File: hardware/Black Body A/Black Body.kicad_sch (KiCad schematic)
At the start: 33 parts, among them IC2 MCP96L00T-E_MX, J1 53307-2471, J2 Conn_01x02, J4 LogicAnalyzer, J5 Conn_02x04_Top_Bottom, J7 Conn_02x03_Top_Bottom

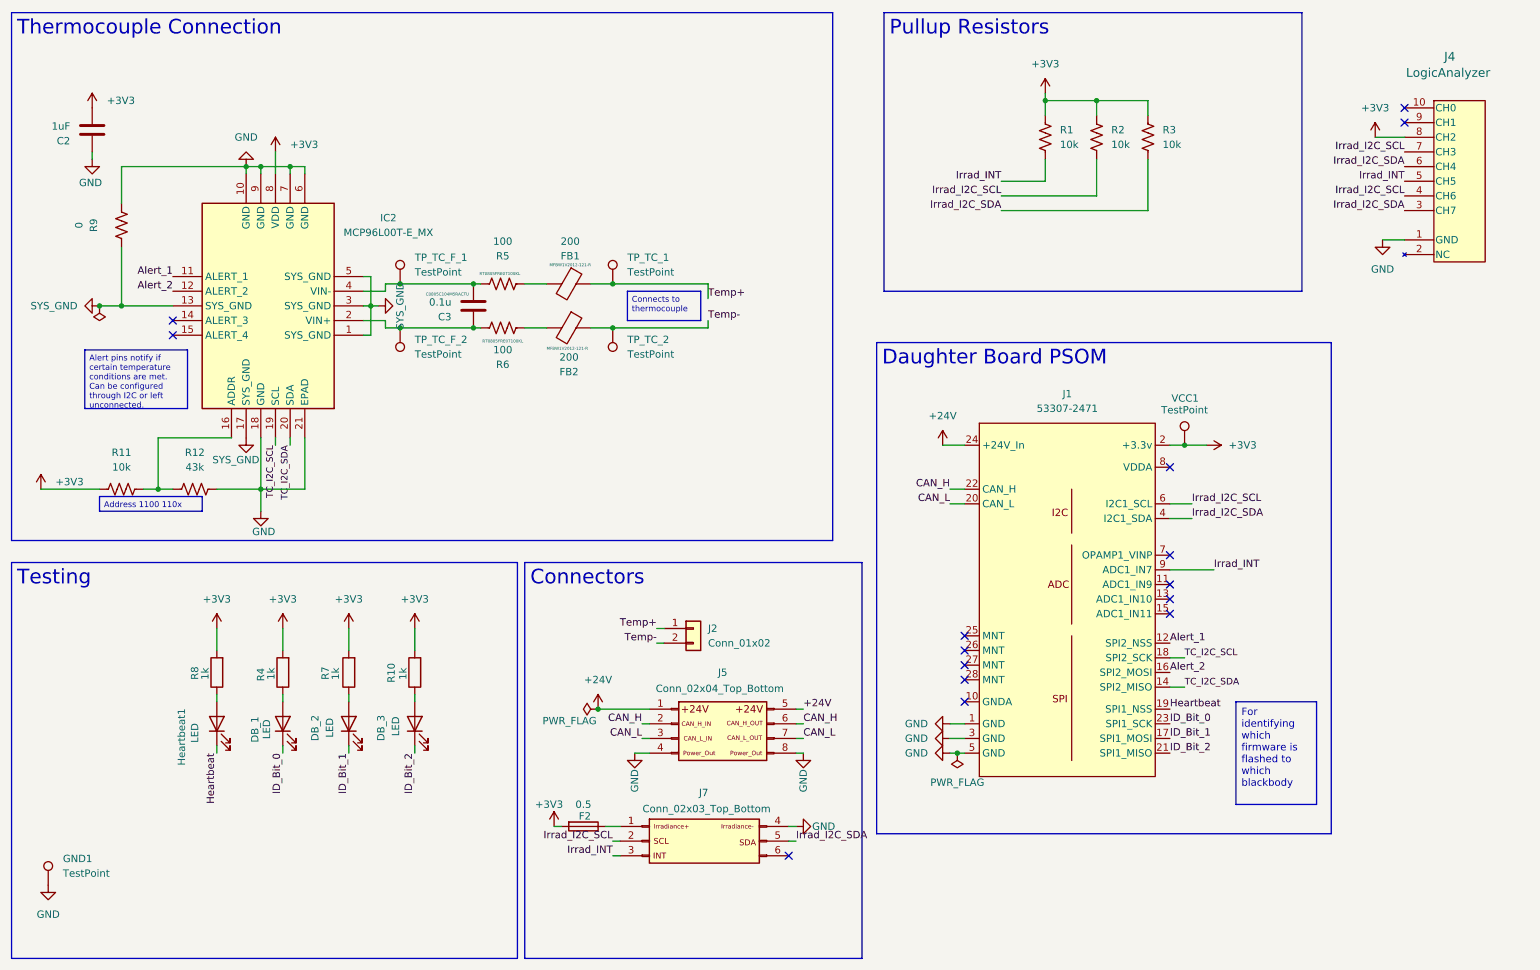
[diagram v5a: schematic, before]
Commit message: updated fuse silkscreen, added open circuit to TC
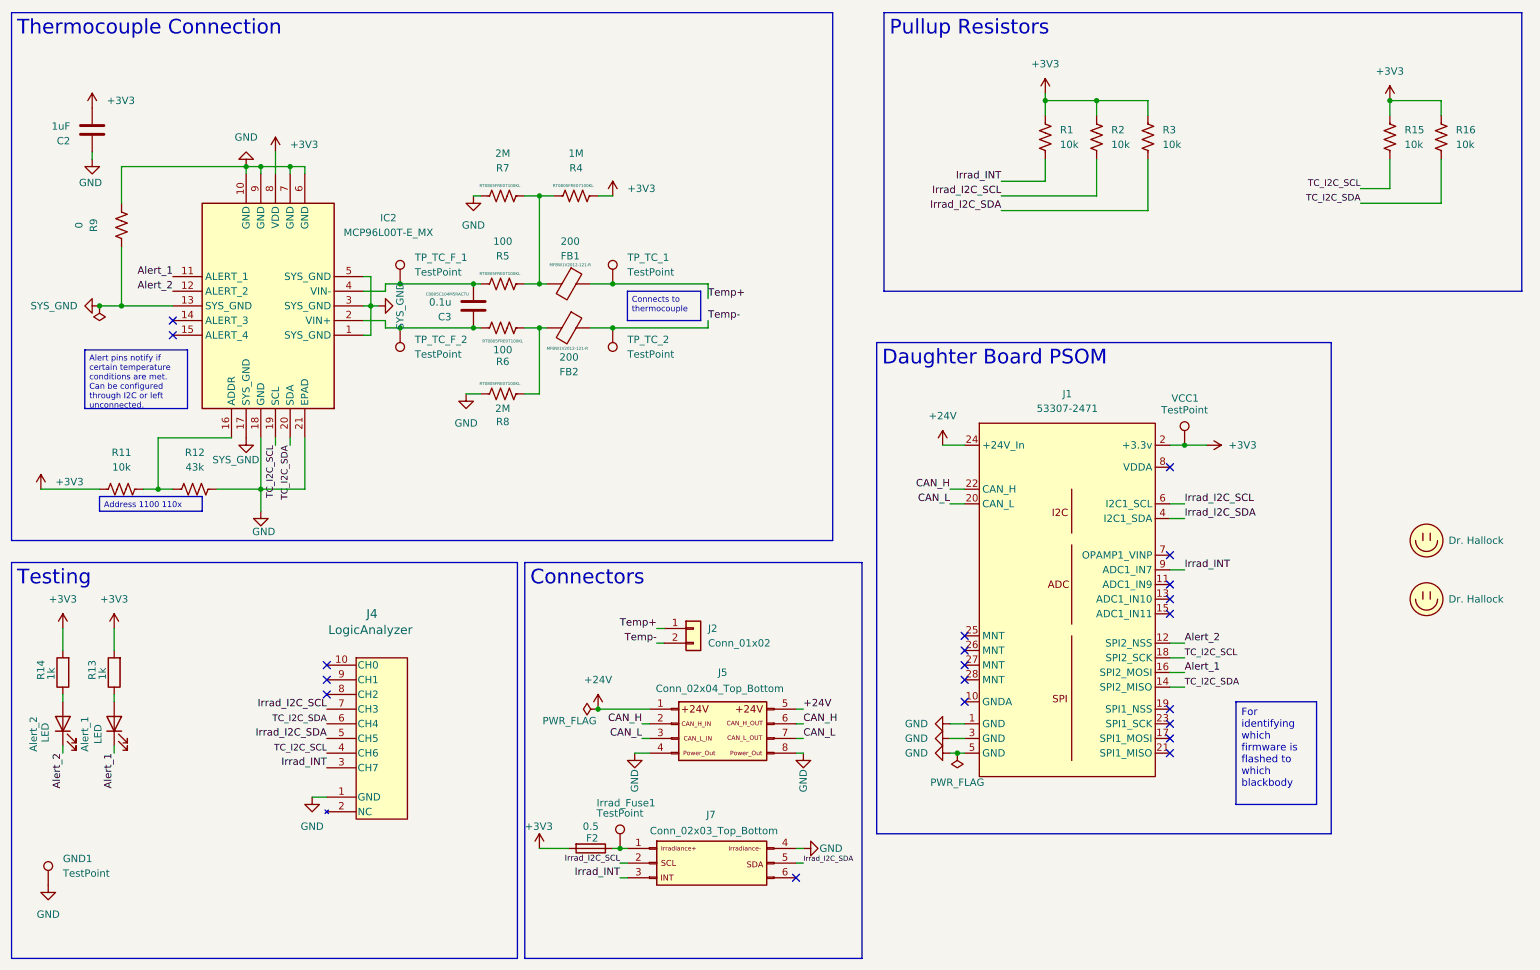
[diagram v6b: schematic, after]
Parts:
- removed DB_1, DB_2, DB_3, Heartbeat1: LED, LED_SMD:LED_0603_1608Metric_Pad1.05x0.95mm_HandSolder, symbol Device:LED
- removed R10, R4, R7, R8: 1k, Resistor_SMD:R_0603_1608Metric_Pad0.98x0.95mm_HandSolder, symbol Device:R
- added Alert_1, Alert_2: LED, LED_SMD:LED_0603_1608Metric_Pad1.05x0.95mm_HandSolder, symbol Device:LED
- added Irrad_Fuse1: TestPoint, TestPoint:TestPoint_Keystone_5005-5009_Compact, symbol Connector:TestPoint
- added LOGO1: Dr. Hallock, utsvt_logos:LHRs_LOGO, symbol utsvt_misc:Logo_Placeholder
- added LOGO2: Dr. Hallock, utsvt_logos:Hallock_Image_Tiny, symbol utsvt_misc:Logo_Placeholder
- added R13, R14: 1k, Resistor_SMD:R_0603_1608Metric_Pad0.98x0.95mm_HandSolder, symbol Device:R
- added R15, R16: 10k, Resistor_SMD:R_0603_1608Metric_Pad0.98x0.95mm_HandSolder, symbol Device:R_US
- added R4: 1M, Resistor_SMD:R_0603_1608Metric_Pad0.98x0.95mm_HandSolder, symbol Device:R_US
- added R7, R8: 2M, Resistor_SMD:R_0603_1608Metric_Pad0.98x0.95mm_HandSolder, symbol Device:R_US
- J1: footprint UTSVT-Conn:PeripheralSOM -> utsvt_connectors:PeripheralSOM
- J4: footprint UTSVT_Connectors:CONN_SFH11-xxxC-D05-ST-XX_SUL -> utsvt_connectors:CONN_SFH11-xxxC-D05-ST-XX_SUL
- R1, R2, R3: footprint Resistor_SMD:R_0805_2012Metric -> Resistor_SMD:R_0603_1608Metric_Pad0.98x0.95mm_HandSolder
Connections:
- net +3V3: now also R13.2, R14.2, R15.1, R16.1, R4.2; no longer J4.8 (CH2)
- net Alert_1: now also J1.16 (SPI2_MOSI), Alert_1.1 (K); no longer J1.12 (SPI2_NSS)
- net Alert_2: now also J1.12 (SPI2_NSS), Alert_2.1 (K); no longer J1.16 (SPI2_MOSI)
- net GND: now also R7.1, R8.1
- net Irrad_I2C_SCL: no longer J4.4 (CH6)
- net Irrad_I2C_SDA: now also J4.5 (CH5); no longer J4.3 (CH7), J4.6 (CH4)
- net Irrad_INT: now also J4.3 (CH7); no longer J4.5 (CH5)
- net TC_I2C_SCL: now also J4.4 (CH6), R15.2
- net TC_I2C_SDA: now also J4.6 (CH4), R16.2
- net at FB1.2, R5.2: now also R4.1, R7.2
- net at FB2.2, R6.2: now also R8.2
- net at F2.1, J7.1 (Pin_1): now also Irrad_Fuse1.1
- net Heartbeat: no longer names the net of J1.19 (SPI1_NSS)
- net ID_Bit_0: no longer names the net of J1.23 (SPI1_SCK)
- net ID_Bit_1: no longer names the net of J1.17 (SPI1_MOSI)
- net ID_Bit_2: no longer names the net of J1.21 (SPI1_MISO)
- new net: Alert_1.2 (A), R13.1
- new net: Alert_2.2 (A), R14.1
- no-connect marks 15 -> 20
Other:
- moved on the sheet: F2, J4, J7

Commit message: updated BOM
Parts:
- J2: P/N (none) -> C17189968
- J5: P/N (none) -> C841208
- J7: P/N (none) -> C493437
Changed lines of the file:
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@@
+			)
+		)
+		(property "P/N" "C841208"
+			(at 132.08 137.16 0)
+			(effects
+				(font
+					(size 1.27 1.27)
+				)
+				(hide yes)
 			)
 		)
@@
 			)
 		)
+		(property "P/N" "C493437"
+			(at 128.27 161.29 0)
+			(effects
+				(font
+					(size 1.27 1.27)
+				)
+				(hide yes)
+			)
+		)
 		(pin "1"
 		)
@@
 			(at 134.62 120.65 0)
 			(effects
+				(font
+					(size 1.27 1.27)
+				)
+				(hide yes)
+			)
+		)
+		(property "P/N" "C17189968"
+			(at 134.62 120.65 0)
+			(effects

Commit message: updated BOM
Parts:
- C2, C3: footprint Capacitor_SMD:C_0805_2012Metric_Pad1.18x1.45mm_HandSolder -> Capacitor_SMD:C_0603_1608Metric_Pad1.08x0.95mm_HandSolder
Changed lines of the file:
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@@
 			)
 		)
-		(property "Footprint" "Capacitor_SMD:C_0805_2012Metric_Pad1.18x1.45mm_HandSolder"
+		(property "Footprint" "Capacitor_SMD:C_0603_1608Metric_Pad1.08x0.95mm_HandSolder"
 			(at 95.5548 60.96 0)
 			(effects
@@
 			)
 		)
-		(property "Footprint" "Capacitor_SMD:C_0805_2012Metric_Pad1.18x1.45mm_HandSolder"
+		(property "Footprint" "Capacitor_SMD:C_0603_1608Metric_Pad1.08x0.95mm_HandSolder"
 			(at 29.5148 30.48 0)
 			(effects
